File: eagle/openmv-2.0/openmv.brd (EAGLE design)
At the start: 25.7 x 35.9 mm, 46 parts, among them U1 OV9650, U10 BEAD, U4 STM32F407LQFP100, X2 USB-MICROB, Y1 12Mhz

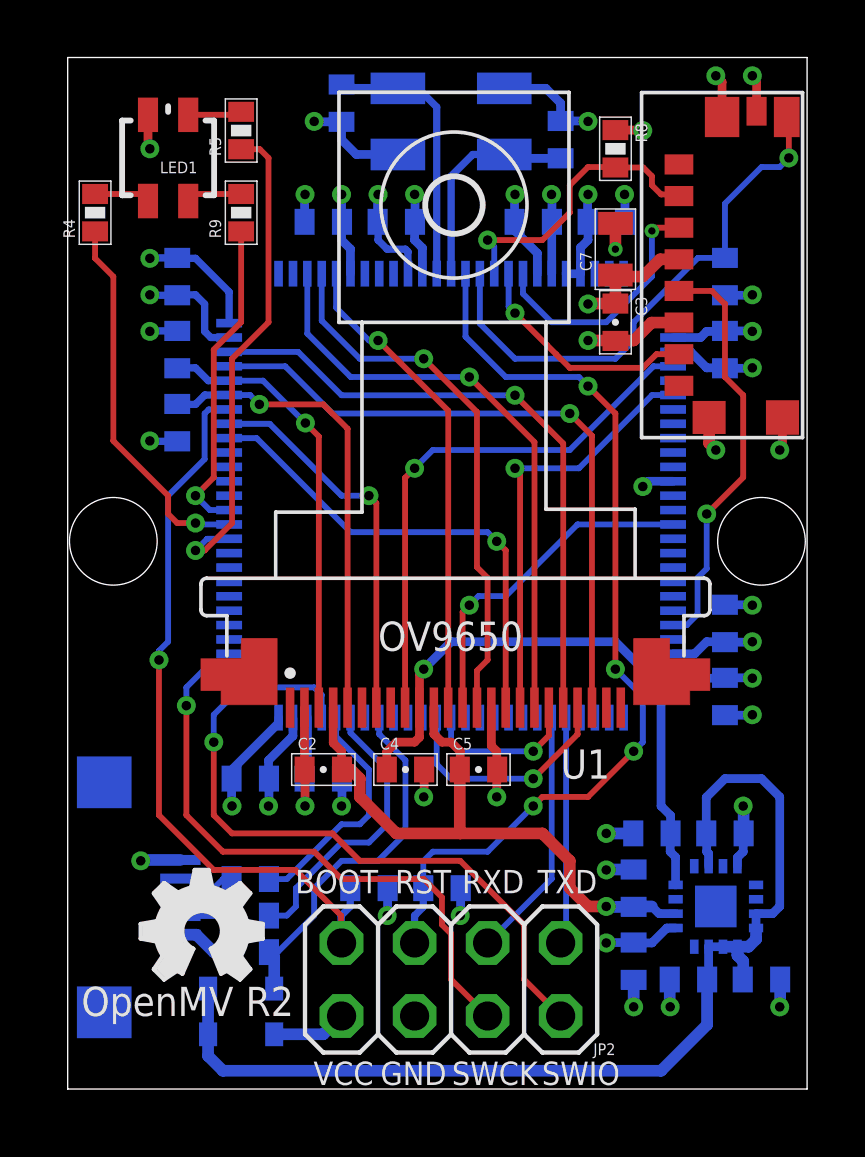
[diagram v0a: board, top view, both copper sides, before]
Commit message: Add test points to breakout SPI3
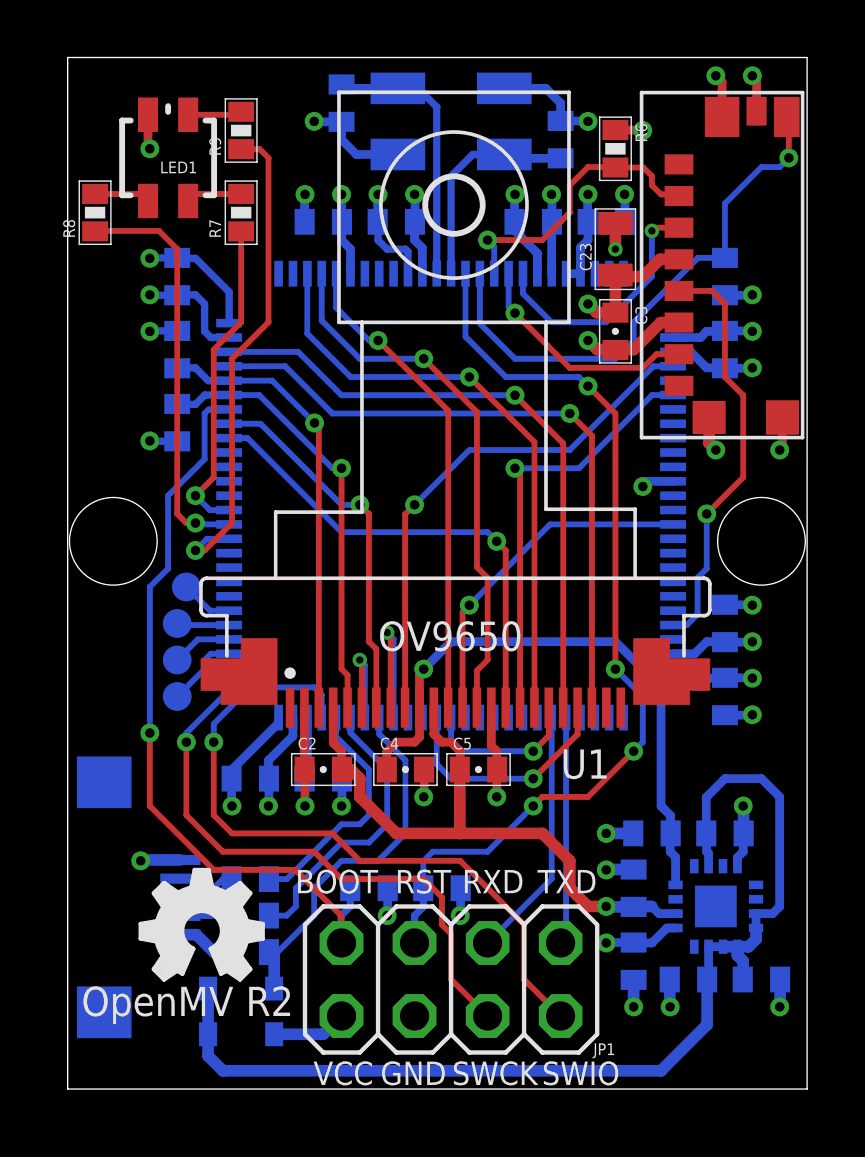
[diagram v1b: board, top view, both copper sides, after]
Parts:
- removed C24: 0.1uF, sfe:0402-CAP
- removed C28, C29: 22pF, sfe:0402-CAP
- added C13, C9: 0.1uF, sfe:0402-CAP
- added C23: 10uF, sfe:0805
- added TP1, TP2, TP3, TP4: TPTP10R, testpad:TP10R
- C10, C11, C14: value 1uF -> 0.1uF
- C16, C19, C20: value 0.1uF -> 1uF
- C21, C22: value 0.1uF -> 22pF
- C7: value 10uF -> 0.1uF; device sfe:0805 -> sfe:0402-CAP
- R1, R2: value 4.7K -> 10K
- R10, R11: value 33 -> 33R
- R4, R5: value 220R -> 10K
- R7, R8: value 10K -> 220R
- moved C10 29.3 mm to (8.89, 30.2)
- moved C20 27.9 mm to (19.7, 4.45), turned to 270 degrees
- moved R5 26.7 mm to (10.5, 6.99), flipped to the bottom, turned to 0 degrees
- moved R6 26.4 mm to (19.1, 32.7), flipped to the top, turned to 270 degrees
- moved R4 26.4 mm to (13.0, 6.99), flipped to the bottom, turned to 180 degrees
- moved C21 24.7 mm to (17.1, 33.0), turned to 90 degrees
- moved C19 24.6 mm to (19.7, 6.99), turned to 90 degrees
- moved R7 23.9 mm to (6.03, 30.5), flipped to the top, turned to 90 degrees
- moved C22 23.5 mm to (9.53, 34.3), turned to 270 degrees
- moved C16 21.9 mm to (21.6, 3.81), turned to 0 degrees
- moved C11 19.1 mm to (6.35, 10.8)
- moved R8 18.2 mm to (0.95, 30.5), turned to 90 degrees
- moved C8 7.30 mm to (11.4, 30.2)
- moved C14 7.30 mm to (22.9, 16.2), turned to 90 degrees
- moved C15 4.49 mm to (24.1, 3.81), turned to 180 degrees
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- renumbered C25 to C6, C26 to C12, JP2 to JP1, R17 to R10, R18 to R11, U$4 to U2, U$9 to U3, U10 to U5, X2 to X1
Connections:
- new net SPI3_MISO: TP3.TP, U4.79
- new net SPI3_MOSI: TP4.TP, U4.80
- new net SPI3_SCLK: TP2.TP, U4.78
- new net SPI3_SSEL: TP1.TP, U4.77
- net 2.8V: now also C19.1; no longer C17.1
- net BOOT0: now also R5.2; no longer R7.2
- net GND: now also C13.2, C16.2, C23.2, C7.1, C8.2, C9.1, R5.1, R6.1; no longer C16.1, C24.2, C28.2, C29.2, C7.2, C8.1, R7.1, R8.1
- net LED_B: now also R8.1; no longer R4.1
- net LED_G: now also R7.1; no longer R9.1
- net LED_R: now also R9.1; no longer R5.1
- net N$10: now also C22.1; no longer C28.1
- net N$16: now also R9.2; no longer R5.2
- net N$6: now also R7.2; no longer R9.2
- net N$7: now also R8.2; no longer R4.2
- net N$9: now also C21.1; no longer C29.1
- net NRST: now also R4.1; no longer R6.1
- net PWDN: now also U4.67
- net RESET: now also U4.69
- net SD_SSEL: now also R6.2; no longer R8.2
- net VCAP1: now also C14.1; no longer C24.1
- net VCAP2: now also C13.1; no longer C22.1
- net VCC: now also C10.1, C11.1, C23.1, C7.2, C8.1, C9.2, R4.2; no longer C15.1, C16.2, C19.1, C21.1, C7.1, C8.2, R6.2
- net VIN: now also C15.1, C16.1, C17.1; no longer C10.1, C11.1, C14.1
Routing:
- net PWDN: track 0.00 -> 5.71 mm, vias 0 -> 1
- net RESET: track 0.00 -> 3.77 mm, vias 0 -> 1
- net SPI3_SSEL: track 0.00 -> 2.61 mm
- net SPI3_SCLK: track 0.00 -> 2.10 mm
- net SPI3_MOSI: track 0.00 -> 1.83 mm
- net SPI3_MISO: track 0.00 -> 1.83 mm
- net LED_B: track 13.2 -> 14.3 mm
- net I2C1_SCL: track 16.3 -> 15.3 mm
- net HSYNC: track 18.9 -> 18.2 mm
